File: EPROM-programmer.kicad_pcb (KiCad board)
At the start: 4 copper layers, 99.1 x 99.1 mm, 63 parts, among them J1 ZIF-socket, J2 ISP, J3 DAC_VCC, J4 DAC_B, J5 GND, J6 Barrel_Jack_Switch, J7 VCC_SEL, J8 AMP_VCC, J9 GND, P1 USB-C, Q1 TIP41C, Q2 BC327, Q3 BC337, SW1 SW_Push, U1 ATmega1284-P, U2 MCP2221AxP, U3 MCP4812, U4 LM358, Y1 20M

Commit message: WIP use LM317
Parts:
- removed J7: VCC_SEL, Connector_PinHeader_2.54mm:PinHeader_1x03_P2.54mm_Vertical
- removed Q3: BC337, Package_TO_SOT_THT:TO-92_Inline_Wide
- removed R18: 2K, Resistor_THT:R_Axial_DIN0207_L6.3mm_D2.5mm_P10.16mm_Horizontal
- added C15: 10u, Local:C_Rect_L4.6mm_W3.0mm_P2.50mm_MKS02_FKP02, F.Cu at (84.1, 155.2)
- added C16: 10u, Local:C_Rect_L4.6mm_W3.0mm_P2.50mm_MKS02_FKP02, F.Cu at (88.5, 139.4)
- added D8: SB340, Diode_THT:D_DO-201AD_P15.24mm_Horizontal, F.Cu at (95.2, 155.6)
- added U5: ULN2003, Package_DIP:DIP-16_W7.62mm_Socket, F.Cu at (111.1, 128.4)
- added U6: LM317_TO-220, Package_TO_SOT_THT:TO-220-3_Vertical, F.Cu at (84.1, 144.8)
- J4: value DAC_B -> DAC_VPP
- Q1: value TIP41C -> BC327; footprint Package_TO_SOT_THT:TO-220-3_Vertical -> Package_TO_SOT_THT:TO-92_Inline_Wide
- R15: value 1K -> 5.1K
- R16: value 2K -> 5.1K
- R17: value 2K -> 240
- moved R11 20.8 mm to (64.1, 145.4), turned to -90 degrees
- moved R17 19.9 mm to (90.2, 145.4)
- moved R12 15.9 mm to (78.7, 154.9)
- moved R15 8.91 mm to (101.0, 139.7), turned to 0 degrees
- moved Q1 8.00 mm to (80.0, 137.5), turned to 0 degrees
- moved R16 4.62 mm to (104.1, 148.6)
- moved TP4 4.62 mm to (104.1, 153.0)
- moved J8 4.62 mm to (108.6, 153.0)
- moved C11 3.86 mm to (57.8, 146.8)
- moved R13 3.42 mm to (81.3, 128.3)
- moved R14 3.42 mm to (71.1, 132.1)
- moved J9 2.54 mm to (59.1, 154.3)
- moved TP5 2.54 mm to (54.6, 154.3)
- moved Q2 1.91 mm to (109.2, 143.5)
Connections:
- Q1 pad 1: Net-(Q1-B) -> GND
- Q1 pad 2: +28V -> Net-(Q1-B)
- Q1 pad 3: /AMP_VCC -> Net-(Q1-E)
- Q2 pad 1: /V_VCC -> /ZIF_VCC
- R17 pad 1: /ZIF_VCC_EN -> /AMP_VCC
- R17 pad 2: Net-(Q3-B) -> Net-(Q1-E)
- U1 pad 2: unconnected-(U1-PB1-Pad2) -> /ZIF_VPP_P21_EN
- U1 pad 3: unconnected-(U1-PB2-Pad3) -> /ZIF_VPP_P22_EN
- U1 pad 4: unconnected-(U1-PB3-Pad4) -> /ZIF_VPP_P23_EN
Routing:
- net /ZIF_VPP_P21_EN: track 0.00 -> 76.9 mm
- net /ZIF_VCC: track 23.7 -> 99.7 mm
- net /V_VCC: track 75.0 -> 0.00 mm
- net /ZIF_VPP_P22_EN: track 0.00 -> 70.5 mm
- net /ZIF_VPP_P23_EN: track 0.00 -> 64.9 mm
- net Net-(Q1-E): track 0.00 -> 27.1 mm
- net +28V: track 53.6 -> 75.1 mm
- net Net-(Q3-B): track 16.6 -> 0.00 mm
- net /AMP_VCC: track 44.9 -> 59.9 mm
- net Net-(U5-O1): track 10.1 -> 3.72 mm
- net Net-(Q1-B): track 24.3 -> 19.1 mm
- net /ZIF_P22: track 73.9 -> 78.0 mm, vias 0 -> 2
- net /ZIF_P23: track 73.6 -> 76.9 mm, vias 0 -> 2
- net /ZIF_VCC_EN: track 79.9 -> 82.9 mm
- net +5V: track 6.20 -> 9.11 mm
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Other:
- board text added: "EPROM-reader V1.2"
- board text removed: "EPROM-reader V1.1"

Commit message: Fix some ERC/DRC
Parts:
- added J7: ZIF_VCC, Connector_PinHeader_2.54mm:PinHeader_1x01_P2.54mm_Vertical, F.Cu at (131.4, 75.6)
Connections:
- net /DAC_B renamed /DAC_VPP
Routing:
- net GND: vias 6 -> 12

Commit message: Fix more DRC-errors
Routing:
- net GND: track 8.09 -> 13.9 mm
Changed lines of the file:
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@@
+	)
+	(segment
+		(start 58.855 64.477)
+		(end 58.855 61.595)
+		(width 0.44)
+		(layer "In2.Cu")
+		(net 2)
+	)
+	(segment
+		(start 52.905 64.477)
+		(end 52.905 61.595)
+		(width 0.44)
+		(layer "In2.Cu")
+		(net 2)
 	)
 	(segment
@@
 	(segment
 		(start 97.79 142.875)
-		(end 98.425 142.875)
+		(end 100.33 142.875)
 		(width 1)
 		(layer "F.Cu")
@@
 		(width 1)
 		(layer "F.Cu")
-		(net 63)
-	)
-	(segment
-		(start 98.425 142.875)
-		(end 100.33 142.875)
-		(width 1)
-		(layer "F.Cu")

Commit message: Minor adjustments
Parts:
- R17: value 240 -> 220
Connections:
- R14 pad 2: /AMP_VCC -> Net-(Q1-E)
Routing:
- net /AMP_VCC: track 59.9 -> 44.8 mm
- net Net-(Q1-E): track 27.1 -> 35.2 mm
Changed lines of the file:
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@@
 			(layers "*.Cu" "*.Mask")
 			(remove_unused_layers no)
-			(net 63 "/AMP_VCC")
+			(net 80 "Net-(Q1-E)")
 			(pintype "passive")
 		)
@@
 			)
 		)
-		(property "Value" "240"
+		(property "Value" "220"
 			(at 5.08 2.37 90)
 			(layer "F.Fab")
@@
 	)
 	(segment
-		(start 86.36 133.35)
-		(end 88.9 133.35)
-		(width 0.25)
-		(layer "F.Cu")
-		(net 63)
-	)
-	(segment
 		(start 87.955 145.415)
 		(end 90.17 145.415)
@@
 	)
 	(segment
-		(start 90.805 139.176)
-		(end 90.543 139.438)
-		(width 0.25)
-		(layer "F.Cu")
-		(net 63)
-	)
-	(segment
-		(start 81.28 132.08)
-		(end 85.09 132.08)
-		(width 0.25)
-		(layer "F.Cu")
-		(net 63)
-	)
-	(segment
 		(start 104.14 143.51)
 		(end 104.14 148.59)
@@
 	)
 	(segment
-		(start 90.805 135.255)
-		(end 90.805 139.176)
-		(width 0.25)
-		(layer "F.Cu")
-		(net 63)
-	)
-	(segment
-		(start 88.9 133.35)
-		(end 90.805 135.255)
-		(width 0.25)
-		(layer "F.Cu")
-		(net 63)
-	)
-	(segment
 		(start 97.79 142.875)
 		(end 100.33 142.875)
@@
 	)
 	(segment
-		(start 85.09 132.08)
-		(end 86.36 133.35)
-		(width 0.25)
-		(layer "F.Cu")
-		(net 63)
-	)
-	(segment
 		(start 87.63 145.74)
 		(end 87.955 145.415)
@@
 	)
 	(segment
+		(start 85.09 133.985)
+		(end 85.09 137.52)
+		(width 0.25)
+		(layer "F.Cu")
+		(net 80)
+	)
+	(segment
 		(start 84.145 144.78)
 		(end 83.185 144.78)
@@
 	)
 	(segment
+		(start 83.185 132.08)
+		(end 85.09 133.985)
+		(width 0.25)
+		(layer "F.Cu")
+		(net 80)
+	)
+	(segment
 		(start 90.17 155.575)
 		(end 90.17 153.035)
@@
 		(width 0.25)
 		(layer "F.Cu")
+		(net 80)
+	)
+	(segment
+		(start 81.28 132.08)
+		(end 83.185 132.08)
+		(width 0.25)
+		(layer "F.Cu")

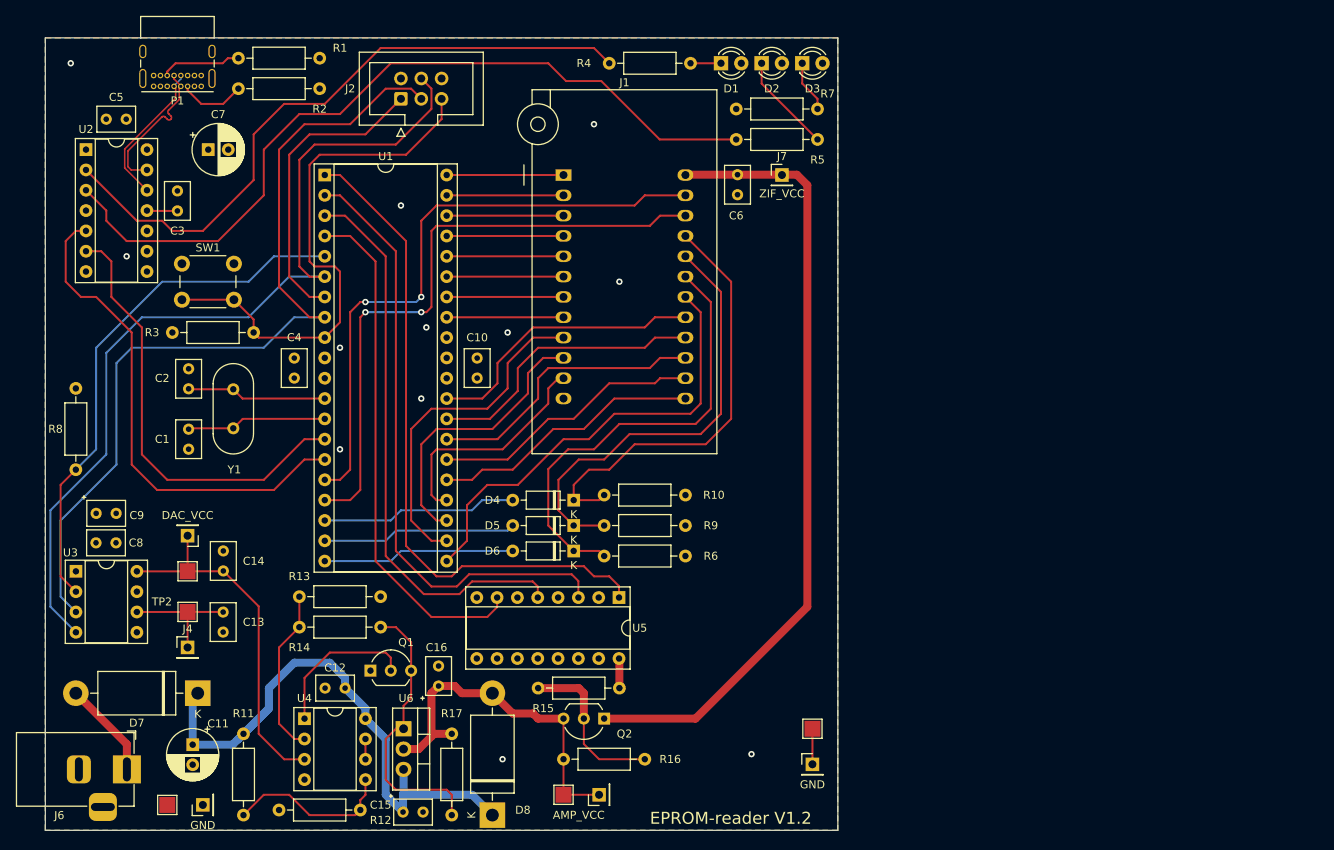
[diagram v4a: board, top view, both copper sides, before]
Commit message: Add LM317 for VPP
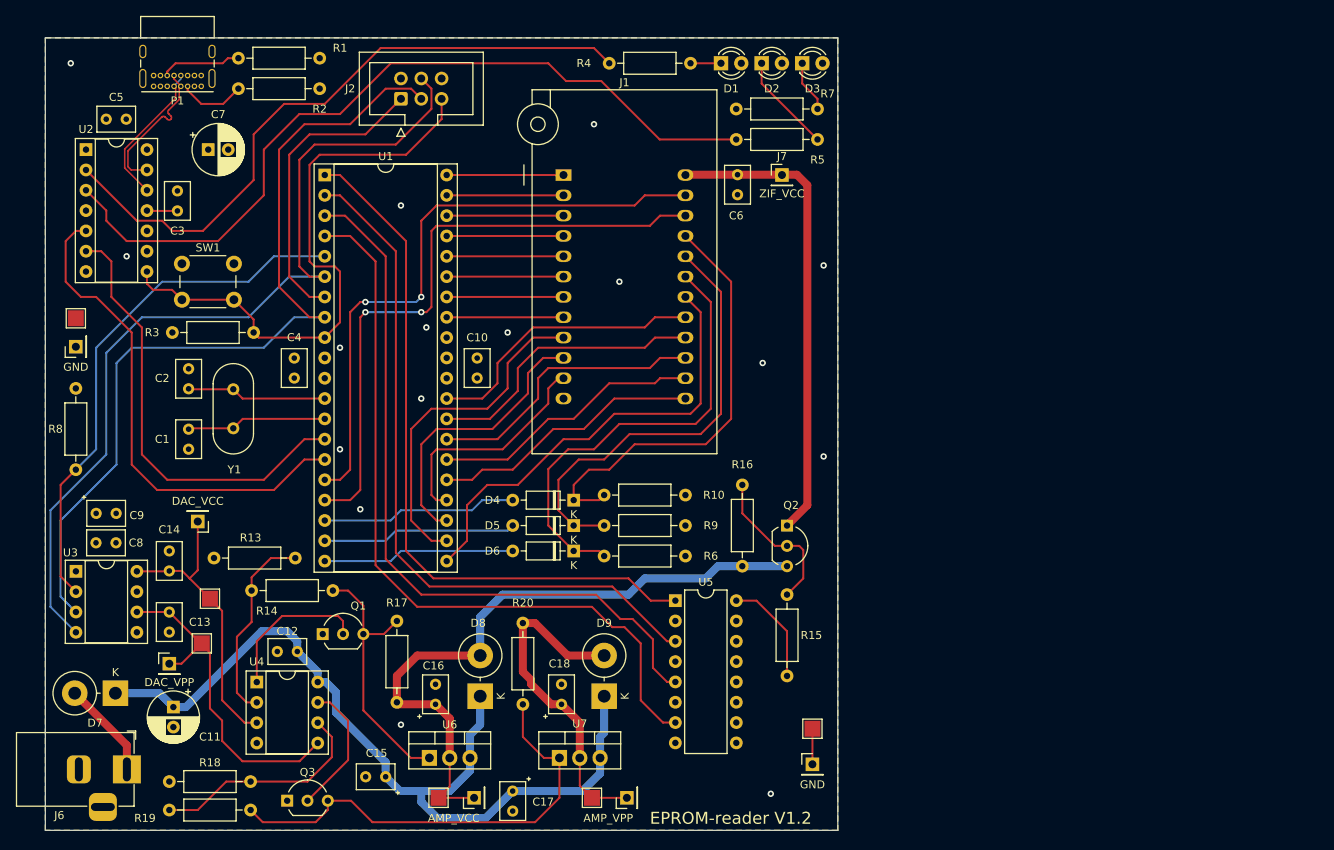
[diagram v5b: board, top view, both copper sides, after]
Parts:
- removed R11, R12: 5K1, Resistor_THT:R_Axial_DIN0207_L6.3mm_D2.5mm_P10.16mm_Horizontal
- added C17: 10u, Local:C_Rect_L4.6mm_W3.0mm_P2.50mm_MKS02_FKP02, F.Cu at (97.8, 152.6)
- added C18: 10u, Local:C_Rect_L4.6mm_W3.0mm_P2.50mm_MKS02_FKP02, F.Cu at (103.9, 141.7)
- added D9: SB340, Diode_THT:D_DO-201AD_P5.08mm_Vertical_KathodeUp, F.Cu at (109.2, 140.7)
- added J10: AMP_VPP, Connector_PinHeader_2.54mm:PinHeader_1x01_P2.54mm_Vertical, F.Cu at (112.1, 153.4)
- added Q3: BC327, Package_TO_SOT_THT:TO-92_Inline_Wide, F.Cu at (69.6, 153.8)
- added R18: 5K6, Resistor_THT:R_Axial_DIN0207_L6.3mm_D2.5mm_P10.16mm_Horizontal, F.Cu at (54.9, 151.4)
- added R19: 82K, Resistor_THT:R_Axial_DIN0207_L6.3mm_D2.5mm_P10.16mm_Horizontal, F.Cu at (54.9, 154.9)
- added R20: 220, Resistor_THT:R_Axial_DIN0207_L6.3mm_D2.5mm_P10.16mm_Horizontal, F.Cu at (99.1, 131.6)
- added TP6: AMP_VPP_TP, TestPoint:TestPoint_Pad_2.0x2.0mm, F.Cu at (107.7, 153.4)
- added U7: LM317_TO-220, Package_TO_SOT_THT:TO-220-3_Vertical, F.Cu at (103.6, 148.4)
- D7, D8: footprint Diode_THT:D_DO-201AD_P15.24mm_Horizontal -> Diode_THT:D_DO-201AD_P5.08mm_Vertical_KathodeUp
- U5: footprint Package_DIP:DIP-16_W7.62mm_Socket -> Package_DIP:DIP-16_W7.62mm
- moved TP5 61.9 mm to (43.2, 93.5)
- moved J9 59.4 mm to (43.2, 97.0)
- moved Q2 33.2 mm to (132.1, 119.4), turned to -90 degrees
- moved R15 33.2 mm to (132.1, 128.0), turned to -90 degrees
- moved R16 32.9 mm to (126.5, 124.5), turned to 90 degrees
- moved R13 21.4 mm to (60.5, 123.4), turned to 0 degrees
- moved J8 15.6 mm to (93.0, 153.4)
- moved TP4 15.6 mm to (88.5, 153.4)
- moved D8 14.9 mm to (93.7, 140.7)
- moved D7 10.3 mm to (48.1, 140.3)
- moved R17 7.91 mm to (83.3, 141.5), turned to 90 degrees
- moved R14 7.52 mm to (65.2, 127.5)
- moved Q1 7.52 mm to (74.0, 132.9)
- moved C12 7.52 mm to (70.9, 135.1)
- moved U4 7.52 mm to (65.8, 138.9)
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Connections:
- net Net-(Q1-E) renamed /ADJ_VCC
- net Net-(U5-O1) renamed /~{ZIF_VCC_EN}
- U2 pad 8: unconnected-(U2-GP3-Pad8) -> /~{RESET}
- U4 pad 5: Net-(U4B-+) -> /DAC_VPP
- U4 pad 6: Net-(U4B--) -> /FB_VPP
- U4 pad 7: Net-(U4B--) -> Net-(Q3-B)
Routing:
- net /ADJ_VPP: track 0.00 -> 58.1 mm
- net /AMP_VPP: track 0.00 -> 42.4 mm
- net /ZIF_VCC: track 99.7 -> 59.4 mm
- net /AMP_VCC: track 44.8 -> 83.0 mm
- net +28V: track 75.1 -> 109.5 mm
- net /ZIF_VPP_P23_EN: track 64.9 -> 95.4 mm
- net /FB_VPP: track 0.00 -> 28.1 mm
- net /DAC_VPP: track 15.2 -> 42.0 mm
- net /ZIF_VPP_P22_EN: track 70.5 -> 92.2 mm
- net Net-(U4B-+): track 21.0 -> 0.00 mm
- net Net-(Q3-B): track 0.00 -> 16.9 mm
- net /ZIF_VPP_P21_EN: track 76.9 -> 89.0 mm
- net /~{ZIF_VCC_EN}: track 3.72 -> 13.5 mm
- net /DAC_VCC: track 44.5 -> 36.9 mm
- net /~{RESET}: track 67.6 -> 74.4 mm
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
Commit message: Very minor adjustments
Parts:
- moved J10 3.05 mm to (109.0, 153.4)
- moved TP6 3.05 mm to (104.6, 153.4)
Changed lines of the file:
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@@
 		(tags "C Rect series Radial pin pitch 2.50mm  length 4.6mm width 3.0mm Capacitor")
 		(property "Reference" "C16"
-			(at 4.818 -0.2565 360)
+			(at 4.818 -0.2565 0)
 			(layer "F.SilkS")
 			(effects
@@
 		(tags "C Rect series Radial pin pitch 2.50mm  length 4.6mm width 3.0mm Capacitor")
 		(property "Reference" "C15"
-			(at 1.135 2.954 360)
+			(at 1.135 2.954 0)
 			(layer "F.SilkS")
 			(effects
@@
 		)
 		(property "Value" "10u"
-			(at 1.25 2.75 360)
+			(at 1.25 2.75 0)
 			(layer "F.Fab")
 			(effects
@@
 		)
 		(property "Footprint" "Local:C_Rect_L4.6mm_W3.0mm_P2.50mm_MKS02_FKP02"
-			(at 0 0 360)
+			(at 0 0 0)
 			(layer "F.Fab")
 			(hide yes)
@@
 		)
 		(property "Datasheet" ""
-			(at 0 0 360)
+			(at 0 0 0)
 			(layer "F.Fab")
 			(hide yes)
@@
 		)
 		(property "Description" "Polarized capacitor"
-			(at 0 0 360)
+			(at 0 0 0)
 			(layer "F.Fab")
 			(hide yes)
@@
 		)
 		(fp_text user "${REFERENCE}"
-			(at 1.25 0 360)
+			(at 1.25 0 0)
 			(layer "F.Fab")
 			(effects
@@
 	(footprint "TestPoint:TestPoint_Pad_2.0x2.0mm"
 		(layer "F.Cu")
-		(at 107.696 153.416)
+		(at 104.648 153.416)
 		(descr "SMD rectangular pad as test Point, square 2.0mm side length")
 		(tags "test point SMD pad rectangle square")
@@
 		(tags "Resistor Axial_DIN0207 series Axial Horizontal pin pitch 10.16mm 0.25W = 1/4W length 6.3mm diameter 2.5mm")
 		(property "Reference" "R19"
-			(at -3.048 1.016 360)
+			(at -3.048 1.016 0)
 			(layer "F.SilkS")
 			(effects
@@
 		)
 		(property "Value" "82K"
-			(at 5.08 2.37 360)
+			(at 5.08 2.37 0)
 			(layer "F.Fab")
 			(effects
@@
 		)
 		(fp_text user "${REFERENCE}"
-			(at 5.08 0 360)
+			(at 5.08 0 0)
 			(layer "F.Fab")
 			(effects
@@
 		(tags "Resistor Axial_DIN0207 series Axial Horizontal pin pitch 10.16mm 0.25W = 1/4W length 6.3mm diameter 2.5mm")
 		(property "Reference" "R17"
-			(at 12.446 0 360)
+			(at 12.446 0 0)
 			(layer "F.SilkS")
 			(effects
@@
 		)
 		(property "Value" "LM317_TO-220"
-			(at 2.54 2.5 360)
+			(at 2.54 2.5 0)
 			(layer "F.Fab")
 			(effects
@@
 	(footprint "Connector_PinHeader_2.54mm:PinHeader_1x01_P2.54mm_Vertical"
 		(layer "F.Cu")
-		(at 112.06 153.416 90)
+		(at 109.012 153.416 90)
 		(descr "Through hole straight pin header, 1x01, 2.54mm pitch, single row")
 		(tags "Through hole pin header THT 1x01 2.54mm single row")
@@
 		)
 		(fp_text user "${REFERENCE}"
-			(at 0 0 360)
+			(at 0 0 0)
 			(layer "F.Fab")
 			(effects
@@
 		(tags "Resistor Axial_DIN0207 series Axial Horizontal pin pitch 10.16mm 0.25W = 1/4W length 6.3mm diameter 2.5mm")
 		(property "Reference" "R18"
-			(at 5.08 -2.37 360)
+			(at 5.08 -2.37 0)
 			(layer "F.SilkS")
 			(effects
@@
 		)
 		(property "Value" "5K6"
-			(at 5.08 2.37 360)
+			(at 5.08 2.37 0)
 			(layer "F.Fab")
 			(effects
@@
 		)
 		(fp_text user "${REFERENCE}"
-			(at 5.08 0 360)
+			(at 5.08 0 0)
 			(layer "F.Fab")
 			(effects
@@
 		(tags "to-92 sc-43 sc-43a sot54 PA33 transistor")
 		(property "Reference" "Q3"
-			(at 2.54 -3.56 360)
+			(at 2.54 -3.56 0)
 			(layer "F.SilkS")
 			(effects
@@
 		)
 		(property "Value" "BC327"
-			(at 2.54 2.79 360)
+			(at 2.54 2.79 0)
 			(layer "F.Fab")
 			(effects
@@
 		)
 		(fp_text user "${REFERENCE}"
-			(at 2.54 0 360)
+			(at 2.54 0 0)
 			(layer "F.Fab")
 			(effects
@@
 		(tags "Resistor Axial_DIN0207 series Axial Horizontal pin pitch 10.16mm 0.25W = 1/4W length 6.3mm diameter 2.5mm")
 		(property "Reference" "R13"
-			(at 4.572 -2.54 360)
+			(at 4.572 -2.54 0)
 			(layer "F.SilkS")
 			(effects
@@
 		)
 		(property "Value" "5K6"
-			(at 5.08 2.37 360)
+			(at 5.08 2.37 0)
 			(layer "F.Fab")
 			(effects
@@
 		)
 		(property "Footprint" "Resistor_THT:R_Axial_DIN0207_L6.3mm_D2.5mm_P10.16mm_Horizontal"
-			(at 0 0 360)
+			(at 0 0 0)
 			(layer "F.Fab")
 			(hide yes)
@@
 		)
 		(property "Datasheet" ""
-			(at 0 0 360)
+			(at 0 0 0)
 			(layer "F.Fab")
 			(hide yes)
@@
 		)
 		(property "Description" ""
-			(at 0 0 360)
+			(at 0 0 0)
 			(layer "F.Fab")
 			(hide yes)
@@
 		)
 		(fp_text user "${REFERENCE}"
-			(at 5.08 0 360)
+			(at 5.08 0 0)
 			(layer "F.Fab")
 			(effects
@@
 	)
 	(segment
-		(start 107.696 153.416)
-		(end 112.06 153.416)
+		(start 104.648 153.416)
+		(end 109.012 153.416)
+		(width 0.25)
+		(layer "F.Cu")
+		(net 78)
+	)
+	(segment
+		(start 104.648 153.416)
+		(end 106.172 151.892)
 		(width 0.25)
 		(layer "F.Cu")
@@
 	)
 	(segment
-		(start 107.696 153.416)
-		(end 106.172 151.892)
-		(width 0.25)
+		(start 100.076 138.684)
+		(end 99.06 137.668)
+		(width 1)
 		(layer "F.Cu")
 		(net 78)
@@
 	)
 	(segment
-		(start 100.076 138.684)
-		(end 99.06 137.668)
-		(width 1)
-		(layer "F.Cu")
-		(net 78)
-	)
-	(segment
 		(start 100.076 139.192)
 		(end 100.076 138.684)
@@
 	)
 	(segment
-		(start 101.6915 148.4275)
-		(end 99.06 145.796)
+		(start 100.584 156.464)
+		(end 101.092 155.956)
 		(width 0.25)
 		(layer "F.Cu")
@@
 	)
 	(segment
-		(start 100.584 156.464)
-		(end 103.632 153.416)
+		(start 101.6915 148.4275)
+		(end 99.06 145.796)
 		(width 0.25)
 		(layer "F.Cu")
@@
 	)
 	(segment
+		(start 101.346 150.7135)
+		(end 103.632 148.4275)
+		(width 0.25)
+		(layer "F.Cu")
+		(net 80)
+	)
+	(segment
 		(start 74.676 153.776)
 		(end 77.576 153.776)
@@
 	)
 	(segment
-		(start 103.632 153.416)
-		(end 103.632 148.4275)
+		(start 101.346 155.702)
+		(end 101.346 150.7135)
+		(width 0.25)
+		(layer "F.Cu")
+		(net 80)
+	)
+	(segment
+		(start 101.092 155.956)
+		(end 101.346 155.702)
 		(width 0.25)
 		(layer "F.Cu")
